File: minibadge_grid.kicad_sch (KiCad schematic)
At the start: 15 parts

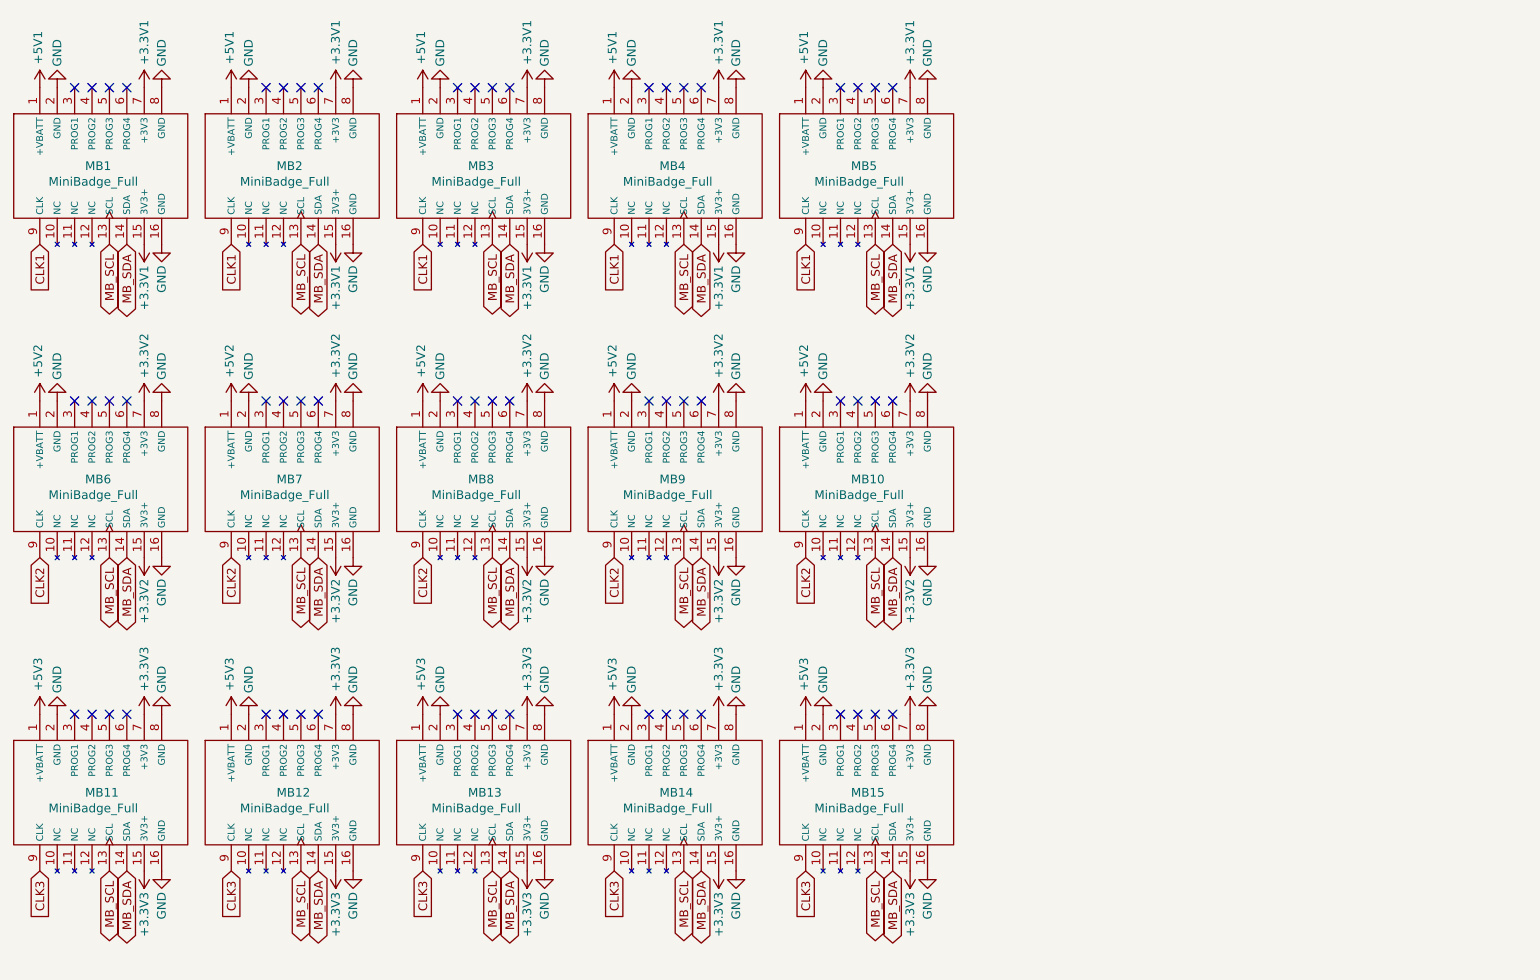
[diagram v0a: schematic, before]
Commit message: flash + bms + usb switch
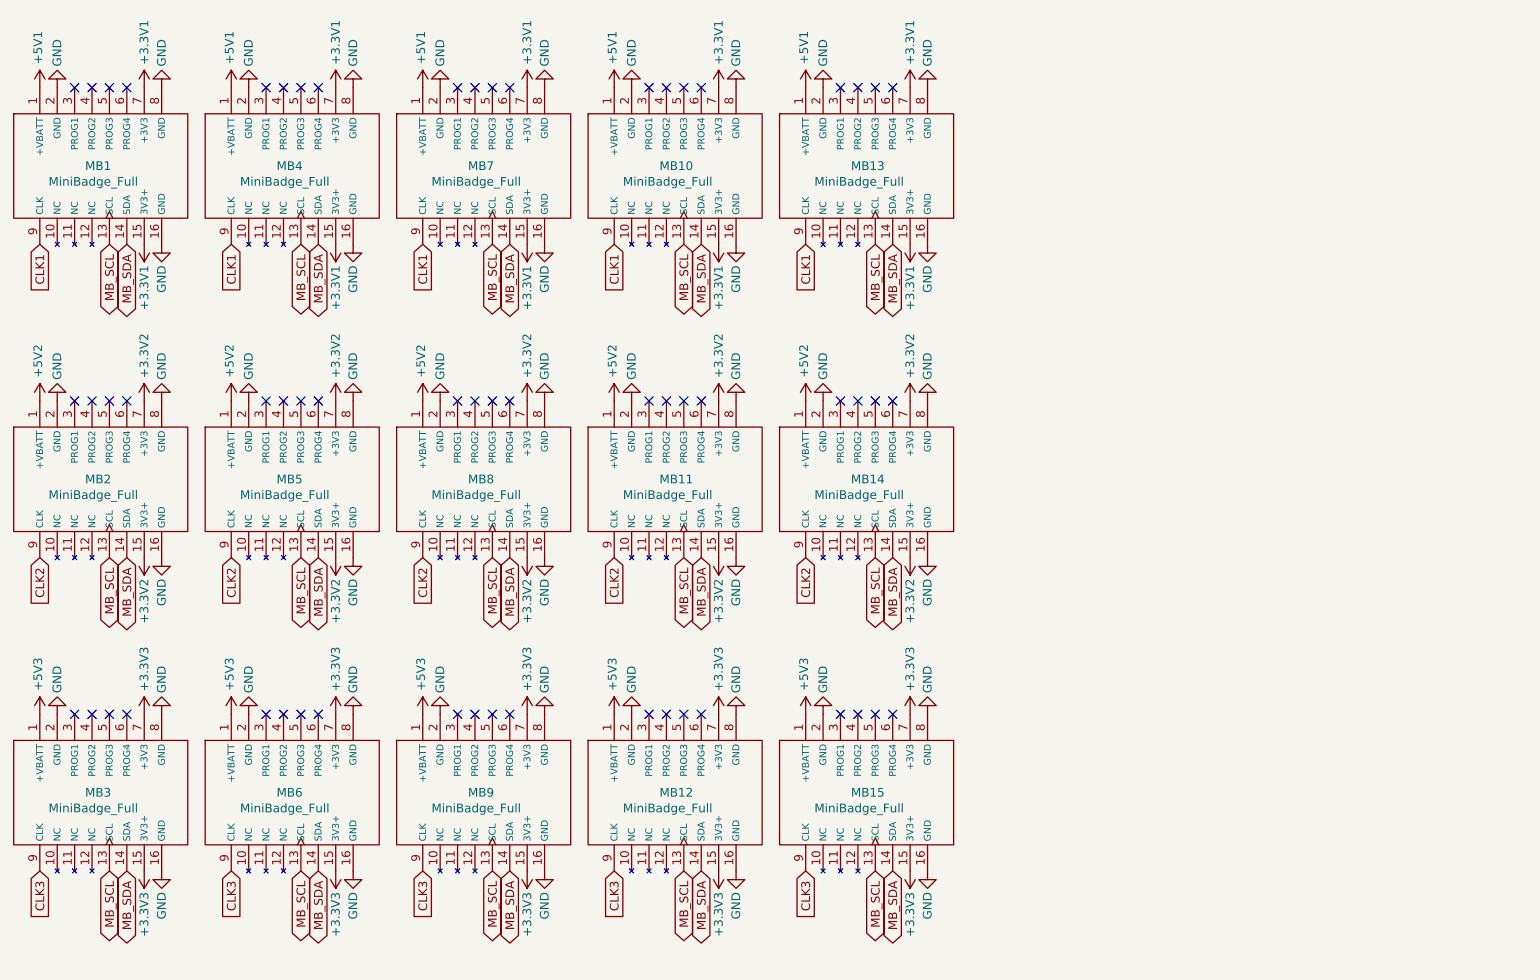
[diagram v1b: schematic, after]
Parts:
- renumbered MB4 to MB10, MB9 to MB11, MB14 to MB12, MB5 to MB13, MB10 to MB14, MB6 to MB2, MB11 to MB3, MB2 to MB4, MB7 to MB5, MB12 to MB6, MB3 to MB7, MB13 to MB9

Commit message: BMS updates
- BMS mostly done
- all BMS pins connected to RP2040
- Re-did Minibadge pinouts
- Connected RP2040 to USB Switch
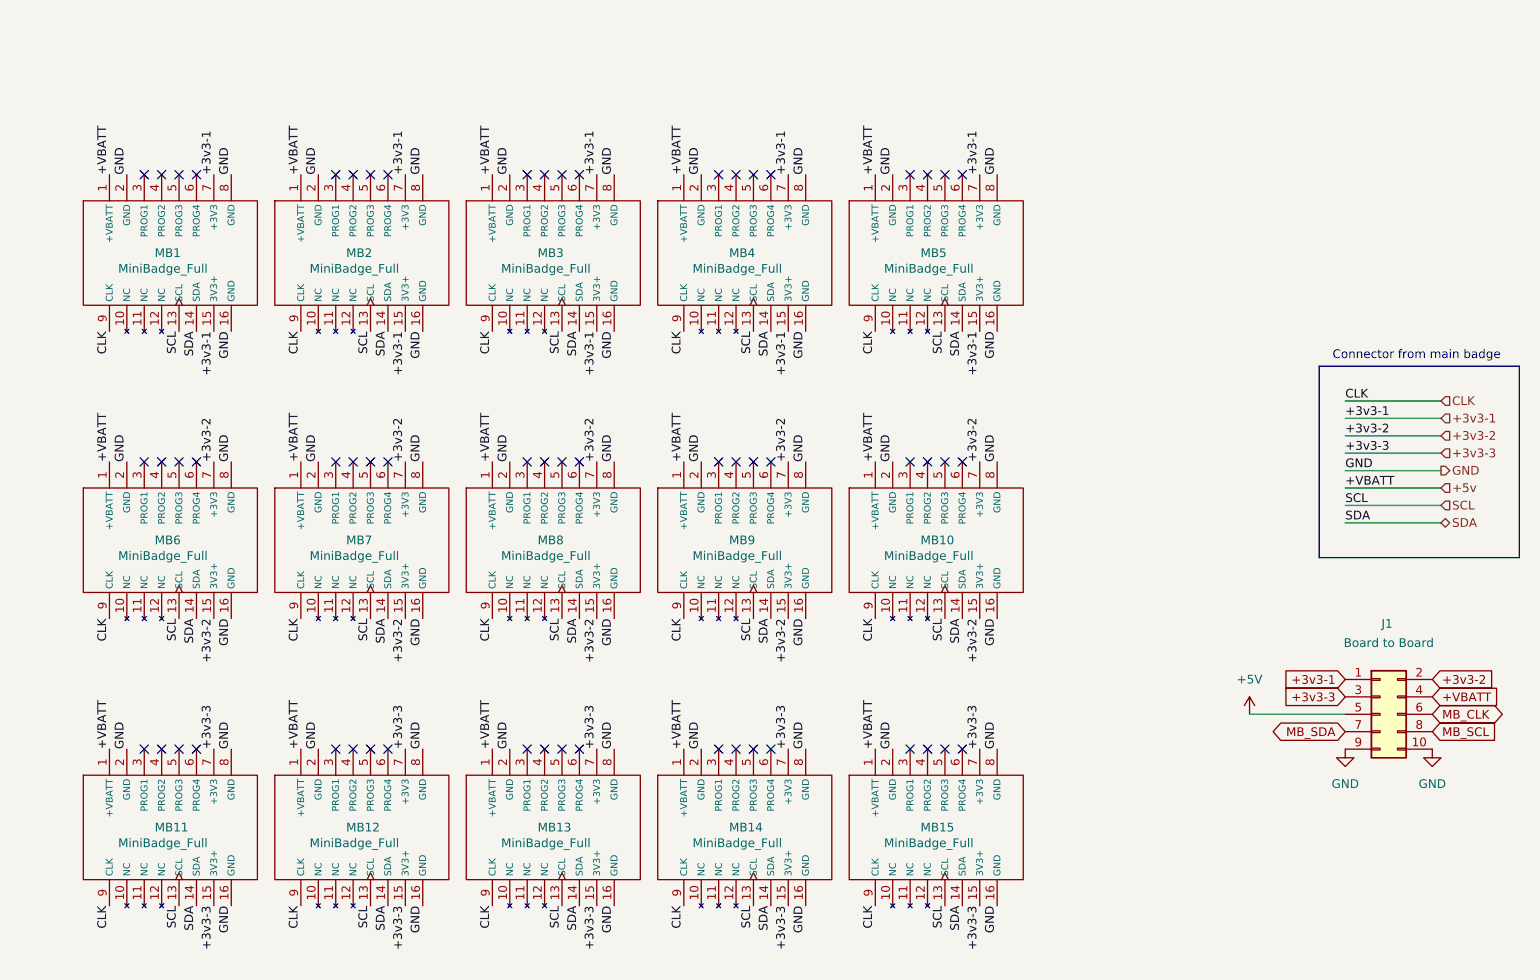
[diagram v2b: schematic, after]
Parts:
- added J1: Board to Board, symbol Connector_Generic:Conn_02x05_Odd_Even
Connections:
- net +5V2 is gone; now on net +VBATT: MB11.1 (+VBATT), MB14.1 (+VBATT), MB2.1 (+VBATT), MB5.1 (+VBATT), MB8.1 (+VBATT)
- net +5V3 is gone; now on net +VBATT: MB12.1 (+VBATT), MB15.1 (+VBATT), MB3.1 (+VBATT), MB6.1 (+VBATT), MB9.1 (+VBATT)
- net CLK2 is gone; now on net CLK: MB11.9 (CLK), MB14.9 (CLK), MB2.9 (CLK), MB5.9 (CLK), MB8.9 (CLK)
- net CLK3 is gone; now on net CLK: MB12.9 (CLK), MB15.9 (CLK), MB3.9 (CLK), MB6.9 (CLK), MB9.9 (CLK)
- net GND: now also J1.10 (Pin_10), J1.9 (Pin_9)
- net MB_SCL: now also J1.8 (Pin_8); no longer MB1.13 (SCL), MB10.13 (SCL), MB11.13 (SCL), MB12.13 (SCL), MB13.13 (SCL), MB14.13 (SCL), MB15.13 (SCL), MB2.13 (SCL), MB3.13 (SCL), MB4.13 (SCL), MB5.13 (SCL), MB6.13 (SCL), MB7.13 (SCL), MB8.13 (SCL), MB9.13 (SCL)
- net MB_SDA: now also J1.7 (Pin_7); no longer MB1.14 (SDA), MB10.14 (SDA), MB11.14 (SDA), MB12.14 (SDA), MB13.14 (SDA), MB14.14 (SDA), MB15.14 (SDA), MB2.14 (SDA), MB3.14 (SDA), MB4.14 (SDA), MB5.14 (SDA), MB6.14 (SDA), MB7.14 (SDA), MB8.14 (SDA), MB9.14 (SDA)
- removed net +3.3V1: MB1.15 (3V3+), MB1.7 (+3V3), MB10.15 (3V3+), MB10.7 (+3V3), MB13.15 (3V3+), MB13.7 (+3V3), MB4.15 (3V3+), MB4.7 (+3V3), MB7.15 (3V3+), MB7.7 (+3V3)
- removed net +3.3V2: MB11.15 (3V3+), MB11.7 (+3V3), MB14.15 (3V3+), MB14.7 (+3V3), MB2.15 (3V3+), MB2.7 (+3V3), MB5.15 (3V3+), MB5.7 (+3V3), MB8.15 (3V3+), MB8.7 (+3V3)
- removed net +3.3V3: MB12.15 (3V3+), MB12.7 (+3V3), MB15.15 (3V3+), MB15.7 (+3V3), MB3.15 (3V3+), MB3.7 (+3V3), MB6.15 (3V3+), MB6.7 (+3V3), MB9.15 (3V3+), MB9.7 (+3V3)
- net +5V1 renamed +VBATT
- net +VBATT: now also J1.4 (Pin_4)
- net CLK1 renamed CLK
- new net +3v3-1: J1.1 (Pin_1), MB1.15 (3V3+), MB1.7 (+3V3), MB2.15 (3V3+), MB2.7 (+3V3), MB3.15 (3V3+), MB3.7 (+3V3), MB4.15 (3V3+), MB4.7 (+3V3), MB5.15 (3V3+), MB5.7 (+3V3)
- new net +3v3-2: J1.2 (Pin_2), MB10.15 (3V3+), MB10.7 (+3V3), MB6.15 (3V3+), MB6.7 (+3V3), MB7.15 (3V3+), MB7.7 (+3V3), MB8.15 (3V3+), MB8.7 (+3V3), MB9.15 (3V3+), MB9.7 (+3V3)
- new net +3v3-3: J1.3 (Pin_3), MB11.15 (3V3+), MB11.7 (+3V3), MB12.15 (3V3+), MB12.7 (+3V3), MB13.15 (3V3+), MB13.7 (+3V3), MB14.15 (3V3+), MB14.7 (+3V3), MB15.15 (3V3+), MB15.7 (+3V3)
- new net +5V: J1.5 (Pin_5)
- new net MB_CLK: J1.6 (Pin_6)
- new net SCL: MB1.13 (SCL), MB10.13 (SCL), MB11.13 (SCL), MB12.13 (SCL), MB13.13 (SCL), MB14.13 (SCL), MB15.13 (SCL), MB2.13 (SCL), MB3.13 (SCL), MB4.13 (SCL), MB5.13 (SCL), MB6.13 (SCL), MB7.13 (SCL), MB8.13 (SCL), MB9.13 (SCL)
- new net SDA: MB1.14 (SDA), MB10.14 (SDA), MB11.14 (SDA), MB12.14 (SDA), MB13.14 (SDA), MB14.14 (SDA), MB15.14 (SDA), MB2.14 (SDA), MB3.14 (SDA), MB4.14 (SDA), MB5.14 (SDA), MB6.14 (SDA), MB7.14 (SDA), MB8.14 (SDA), MB9.14 (SDA)
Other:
- note added: "Connector from main badge"
- moved on the sheet: MB1

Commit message: cleanup
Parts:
- removed J1: Board to Board, symbol Connector_Generic:Conn_02x05_Odd_Even
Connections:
- net +VBATT renamed +5v

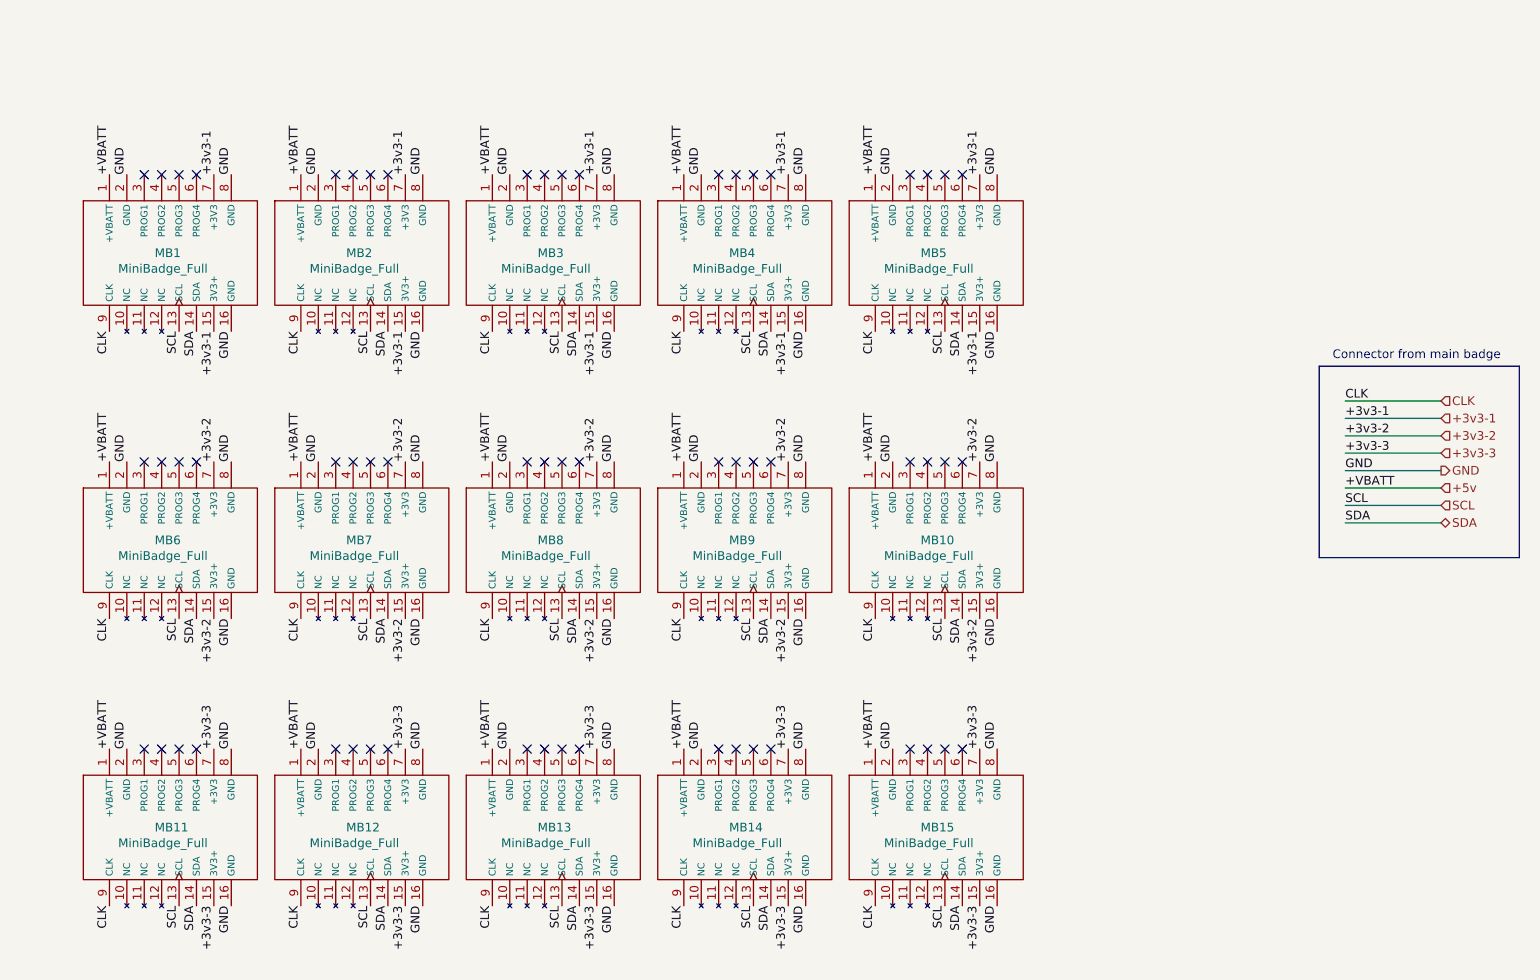
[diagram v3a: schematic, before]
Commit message: BMS updates
Added missing capacitor for OTG
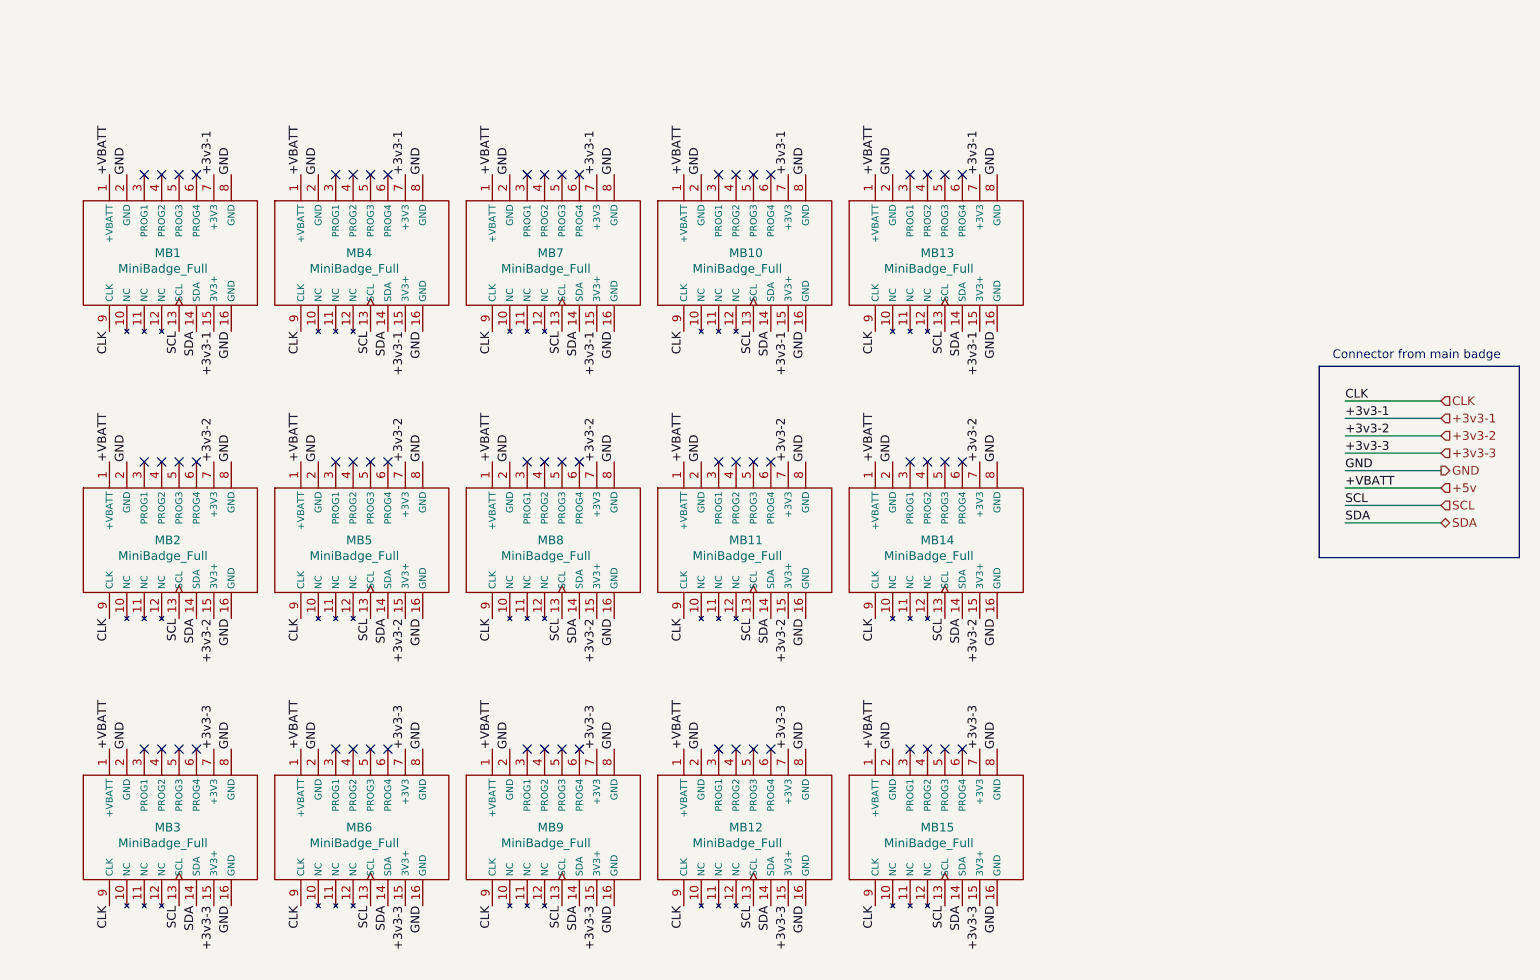
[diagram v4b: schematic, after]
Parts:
- renumbered MB4 to MB10, MB9 to MB11, MB14 to MB12, MB5 to MB13, MB10 to MB14, MB6 to MB2, MB11 to MB3, MB2 to MB4, MB7 to MB5, MB12 to MB6, MB3 to MB7, MB13 to MB9
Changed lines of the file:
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@@
 		(on_board yes)
 		(dnp no)
-		(property "Reference" "MB13"
+		(property "Reference" "MB9"
 			(at 96.774 137.16 0)
 			(effects
@@
 			(project "Minibadge Display 5x3"
 				(path "/e5119d15-74fb-4259-abbc-5cab1f368532/6e97fb62-2d35-4554-a843-3cbb1f9f2f26"
-					(reference "MB13")
+					(reference "MB9")
 					(unit 1)
 				)
@@
 		(on_board yes)
 		(dnp no)
-		(property "Reference" "MB2"
+		(property "Reference" "MB4"
 			(at 68.834 53.34 0)
 			(effects
@@
 			(project "Minibadge Display 5x3"
 				(path "/e5119d15-74fb-4259-abbc-5cab1f368532/6e97fb62-2d35-4554-a843-3cbb1f9f2f26"
-					(reference "MB2")
+					(reference "MB4")
 					(unit 1)
 				)
@@
 		(on_board yes)
 		(dnp no)
-		(property "Reference" "MB5"
+		(property "Reference" "MB13"
 			(at 152.654 53.34 0)
 			(effects
@@
 			(project "Minibadge Display 5x3"
 				(path "/e5119d15-74fb-4259-abbc-5cab1f368532/6e97fb62-2d35-4554-a843-3cbb1f9f2f26"
-					(reference "MB5")
+					(reference "MB13")
 					(unit 1)
 				)
@@
 		(on_board yes)
 		(dnp no)
-		(property "Reference" "MB12"
+		(property "Reference" "MB6"
 			(at 68.834 137.16 0)
 			(effects
@@
 			(project "Minibadge Display 5x3"
 				(path "/e5119d15-74fb-4259-abbc-5cab1f368532/6e97fb62-2d35-4554-a843-3cbb1f9f2f26"
-					(reference "MB12")
+					(reference "MB6")
 					(unit 1)
 				)
@@
 		(on_board yes)
 		(dnp no)
-		(property "Reference" "MB4"
+		(property "Reference" "MB10"
 			(at 124.714 53.34 0)
 			(effects
@@
 			(project "Minibadge Display 5x3"
 				(path "/e5119d15-74fb-4259-abbc-5cab1f368532/6e97fb62-2d35-4554-a843-3cbb1f9f2f26"
-					(reference "MB4")
+					(reference "MB10")
 					(unit 1)
 				)
@@
 		(on_board yes)
 		(dnp no)
-		(property "Reference" "MB14"
+		(property "Reference" "MB12"
 			(at 124.714 137.16 0)
 			(effects
@@
 			(project "Minibadge Display 5x3"
 				(path "/e5119d15-74fb-4259-abbc-5cab1f368532/6e97fb62-2d35-4554-a843-3cbb1f9f2f26"
-					(reference "MB14")
+					(reference "MB12")
 					(unit 1)
 				)
@@
 		(on_board yes)
 		(dnp no)
-		(property "Reference" "MB3"
+		(property "Reference" "MB7"
 			(at 96.774 53.34 0)
 			(effects
@@
 			(project "Minibadge Display 5x3"
 				(path "/e5119d15-74fb-4259-abbc-5cab1f368532/6e97fb62-2d35-4554-a843-3cbb1f9f2f26"
-					(reference "MB3")
+					(reference "MB7")
 					(unit 1)
 				)
@@
 		(on_board yes)
 		(dnp no)
-		(property "Reference" "MB10"
+		(property "Reference" "MB14"
 			(at 152.654 95.25 0)
 			(effects
@@
 			(project "Minibadge Display 5x3"
 				(path "/e5119d15-74fb-4259-abbc-5cab1f368532/6e97fb62-2d35-4554-a843-3cbb1f9f2f26"
-					(reference "MB10")
+					(reference "MB14")
 					(unit 1)
 				)
@@
 		(on_board yes)
 		(dnp no)
-		(property "Reference" "MB6"
+		(property "Reference" "MB2"
 			(at 40.894 95.25 0)
 			(effects
@@
 			(project "Minibadge Display 5x3"
 				(path "/e5119d15-74fb-4259-abbc-5cab1f368532/6e97fb62-2d35-4554-a843-3cbb1f9f2f26"
-					(reference "MB6")
+					(reference "MB2")
 					(unit 1)
 				)
@@
 		(on_board yes)
 		(dnp no)
-		(property "Reference" "MB11"
+		(property "Reference" "MB3"
 			(at 40.894 137.16 0)
 			(effects
@@
 			(project "Minibadge Display 5x3"
 				(path "/e5119d15-74fb-4259-abbc-5cab1f368532/6e97fb62-2d35-4554-a843-3cbb1f9f2f26"
-					(reference "MB11")
+					(reference "MB3")
 					(unit 1)
 				)
@@
 		(on_board yes)
 		(dnp no)
-		(property "Reference" "MB9"
+		(property "Reference" "MB11"
 			(at 124.714 95.25 0)
 			(effects
@@
 			(project "Minibadge Display 5x3"
 				(path "/e5119d15-74fb-4259-abbc-5cab1f368532/6e97fb62-2d35-4554-a843-3cbb1f9f2f26"
-					(reference "MB9")
+					(reference "MB11")
 					(unit 1)
 				)
@@
 		(on_board yes)
 		(dnp no)
-		(property "Reference" "MB7"
+		(property "Reference" "MB5"
 			(at 68.834 95.25 0)
 			(effects
@@
 			(project "Minibadge Display 5x3"
 				(path "/e5119d15-74fb-4259-abbc-5cab1f368532/6e97fb62-2d35-4554-a843-3cbb1f9f2f26"
-					(reference "MB7")
+					(reference "MB5")
 					(unit 1)
 				)
